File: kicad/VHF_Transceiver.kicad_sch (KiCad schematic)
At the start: 16 parts

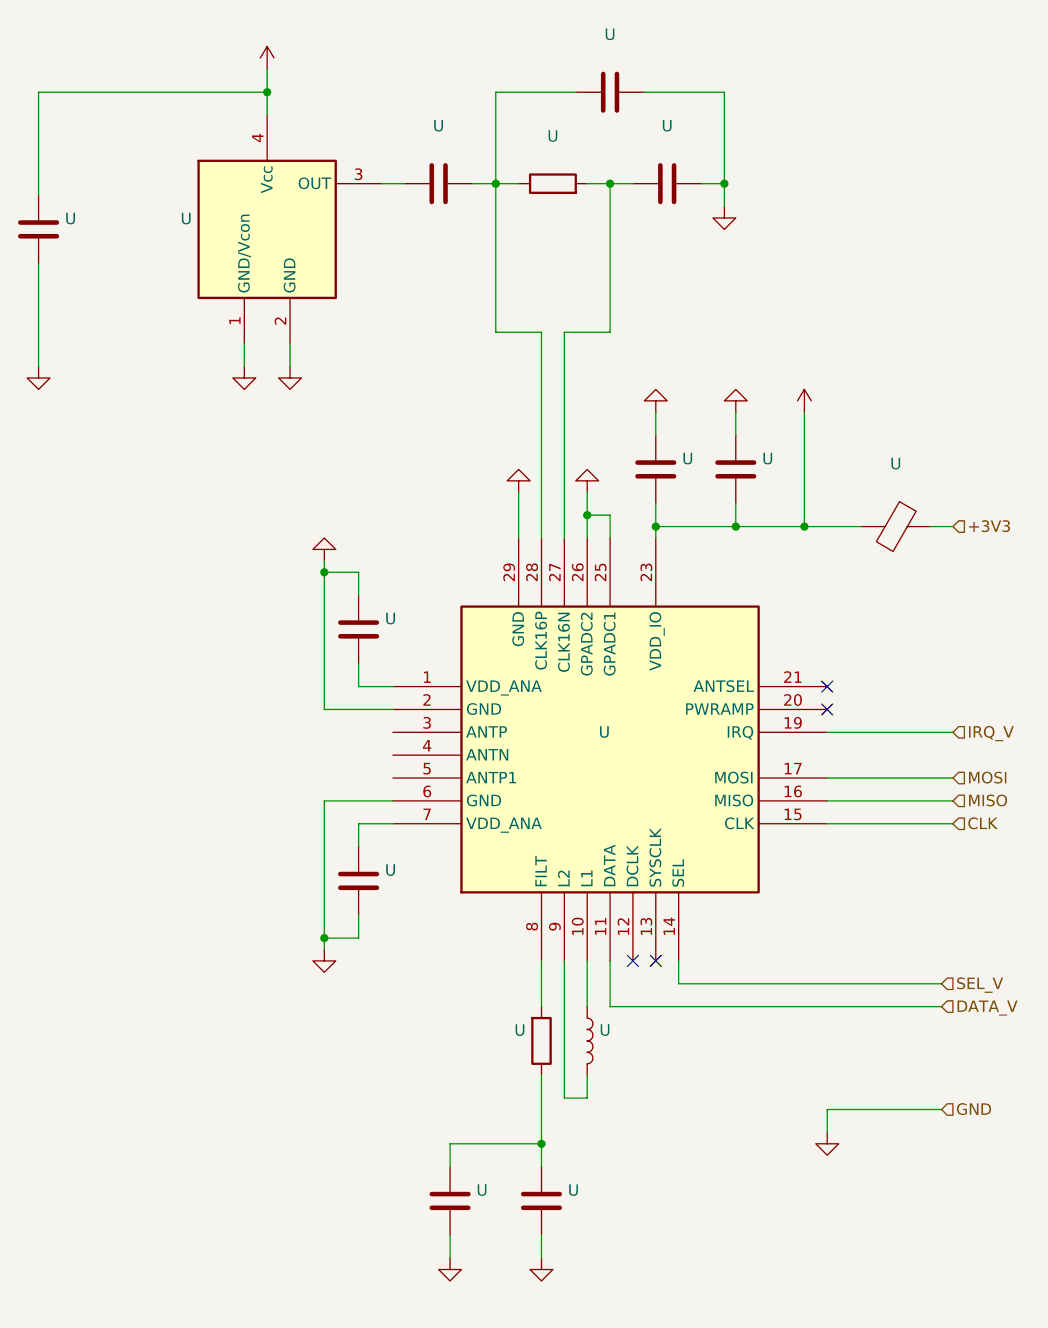
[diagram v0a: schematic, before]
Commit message: Adding PIB USB BRIDGE UML state diagrams - WIP
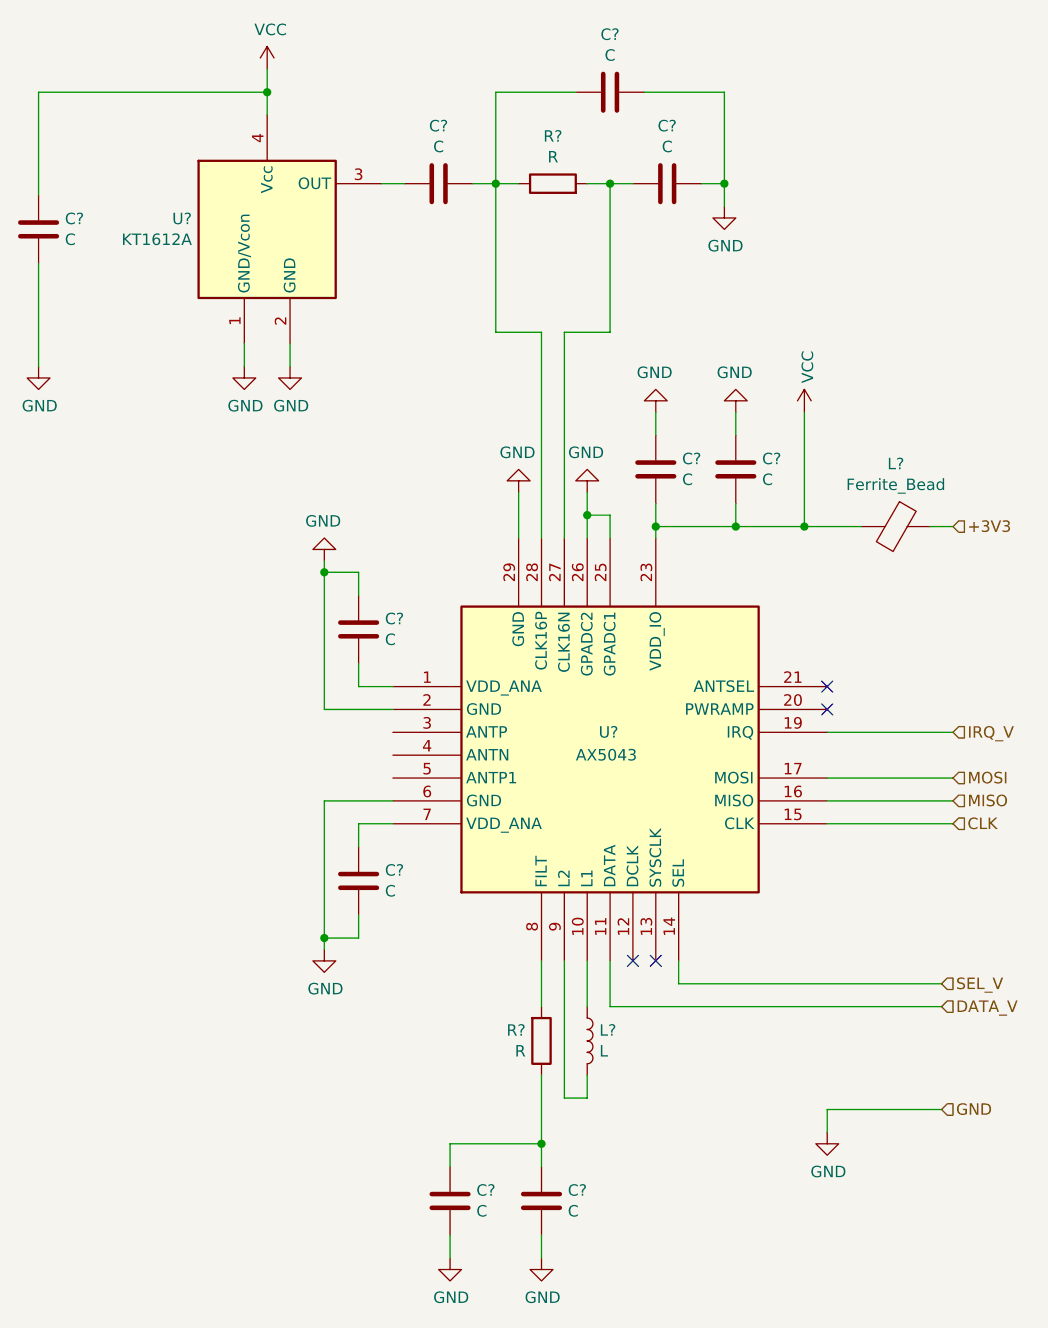
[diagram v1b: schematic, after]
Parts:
- C? (x10): renamed from U; value (none) -> C; symbol device:C -> RCTX-rescue:C-device
- L?: renamed from U; value (none) -> L; symbol device:L -> RCTX-rescue:L-device
- L?: renamed from U; value (none) -> Ferrite_Bead; symbol device:Ferrite_Bead -> RCTX-rescue:Ferrite_Bead-device
- R? (x2): renamed from U; value (none) -> R; symbol device:R -> RCTX-rescue:R-device
- U?: renamed from U; value (none) -> AX5043; footprint (none) -> Housings_DFN_QFN:QFN-28-1EP_5x5mm_Pitch0.5mm; symbol AX5043:AX5043 -> RCTX-rescue:AX5043-AX5043
- U?: renamed from U; value (none) -> KT1612A; footprint (none) -> lsf-kicad-lib:KT1612; symbol KT1612a:KT1612A -> RCTX-rescue:KT1612A-KT1612a
